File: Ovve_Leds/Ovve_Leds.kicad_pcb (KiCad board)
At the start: 2 copper layers, 100 x 150 mm, 57 parts, among them J1 Conn_01x04, J2 Conn_01x04, J3 Conn_01x04, J4 Conn_01x04, J8 Conn_01x02, U1 74LS174

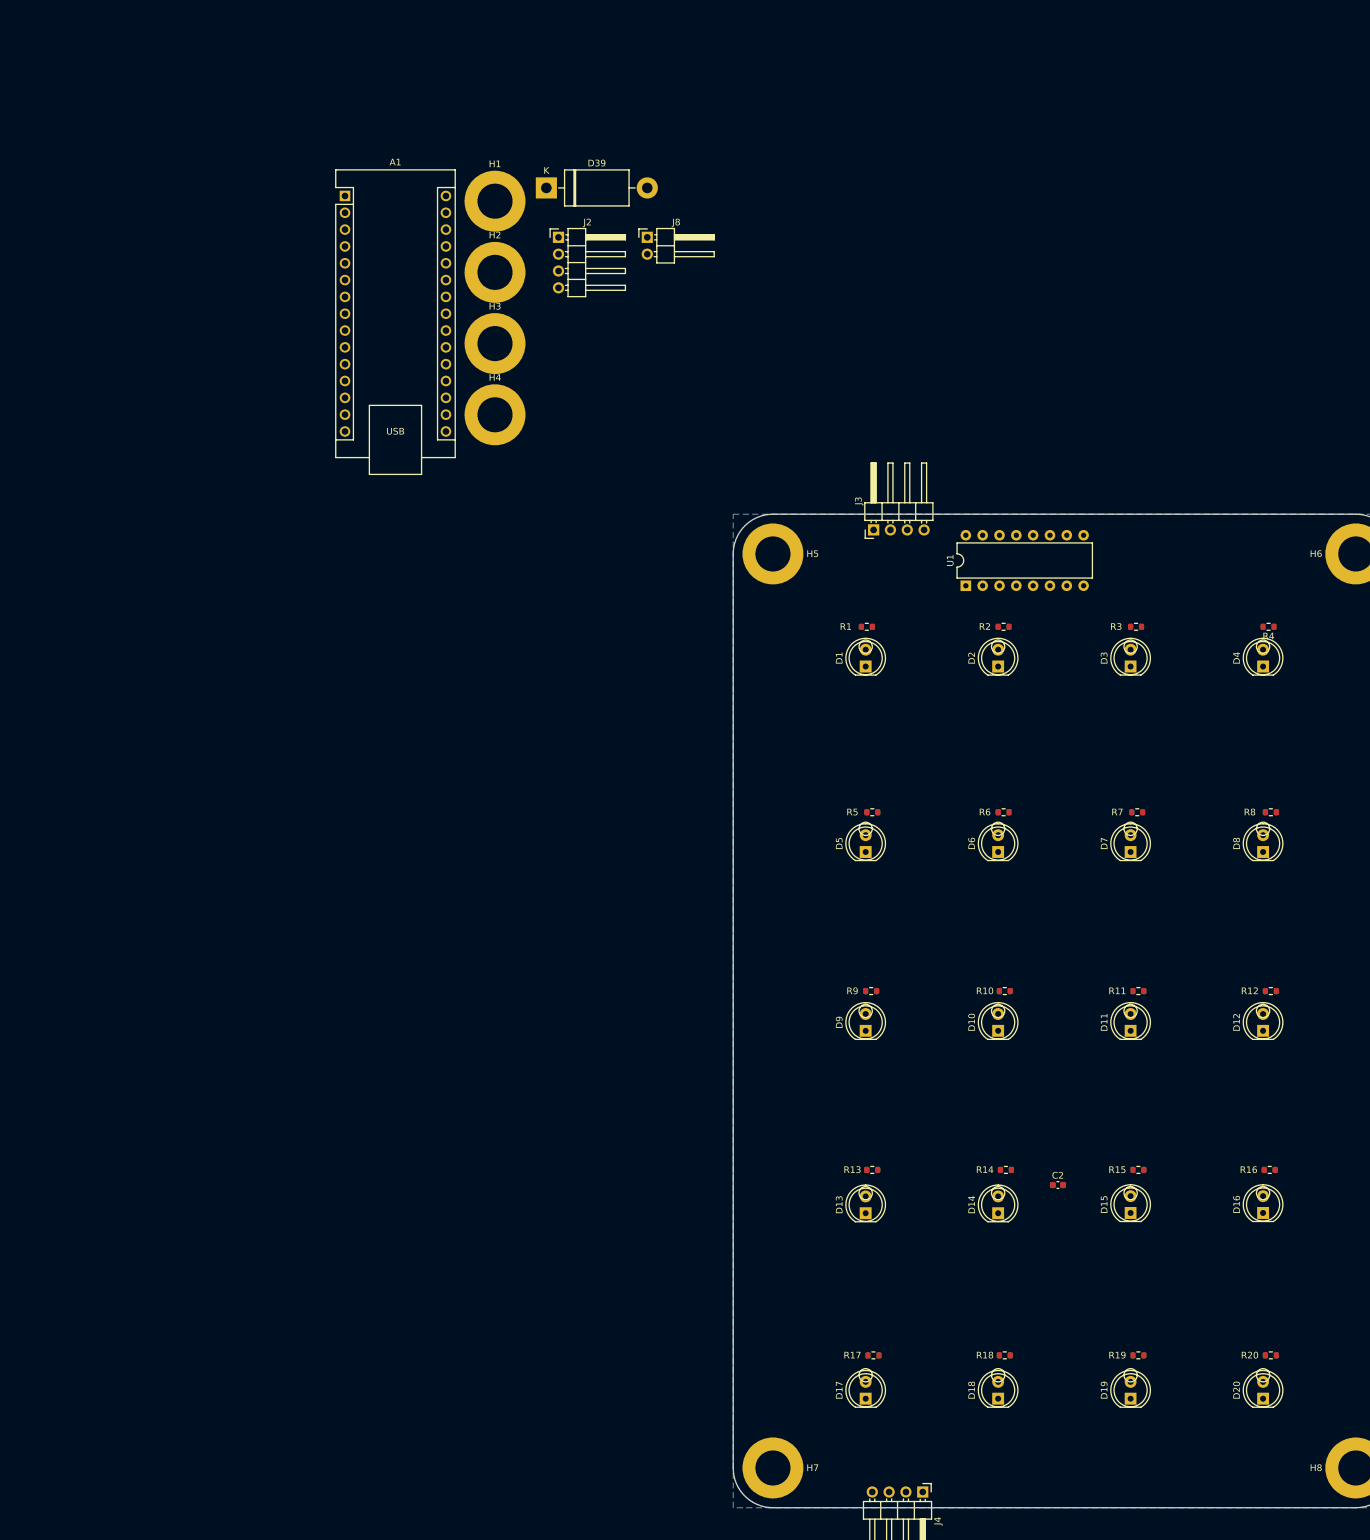
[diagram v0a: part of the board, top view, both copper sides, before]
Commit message: Preliminarily finished with routing letter
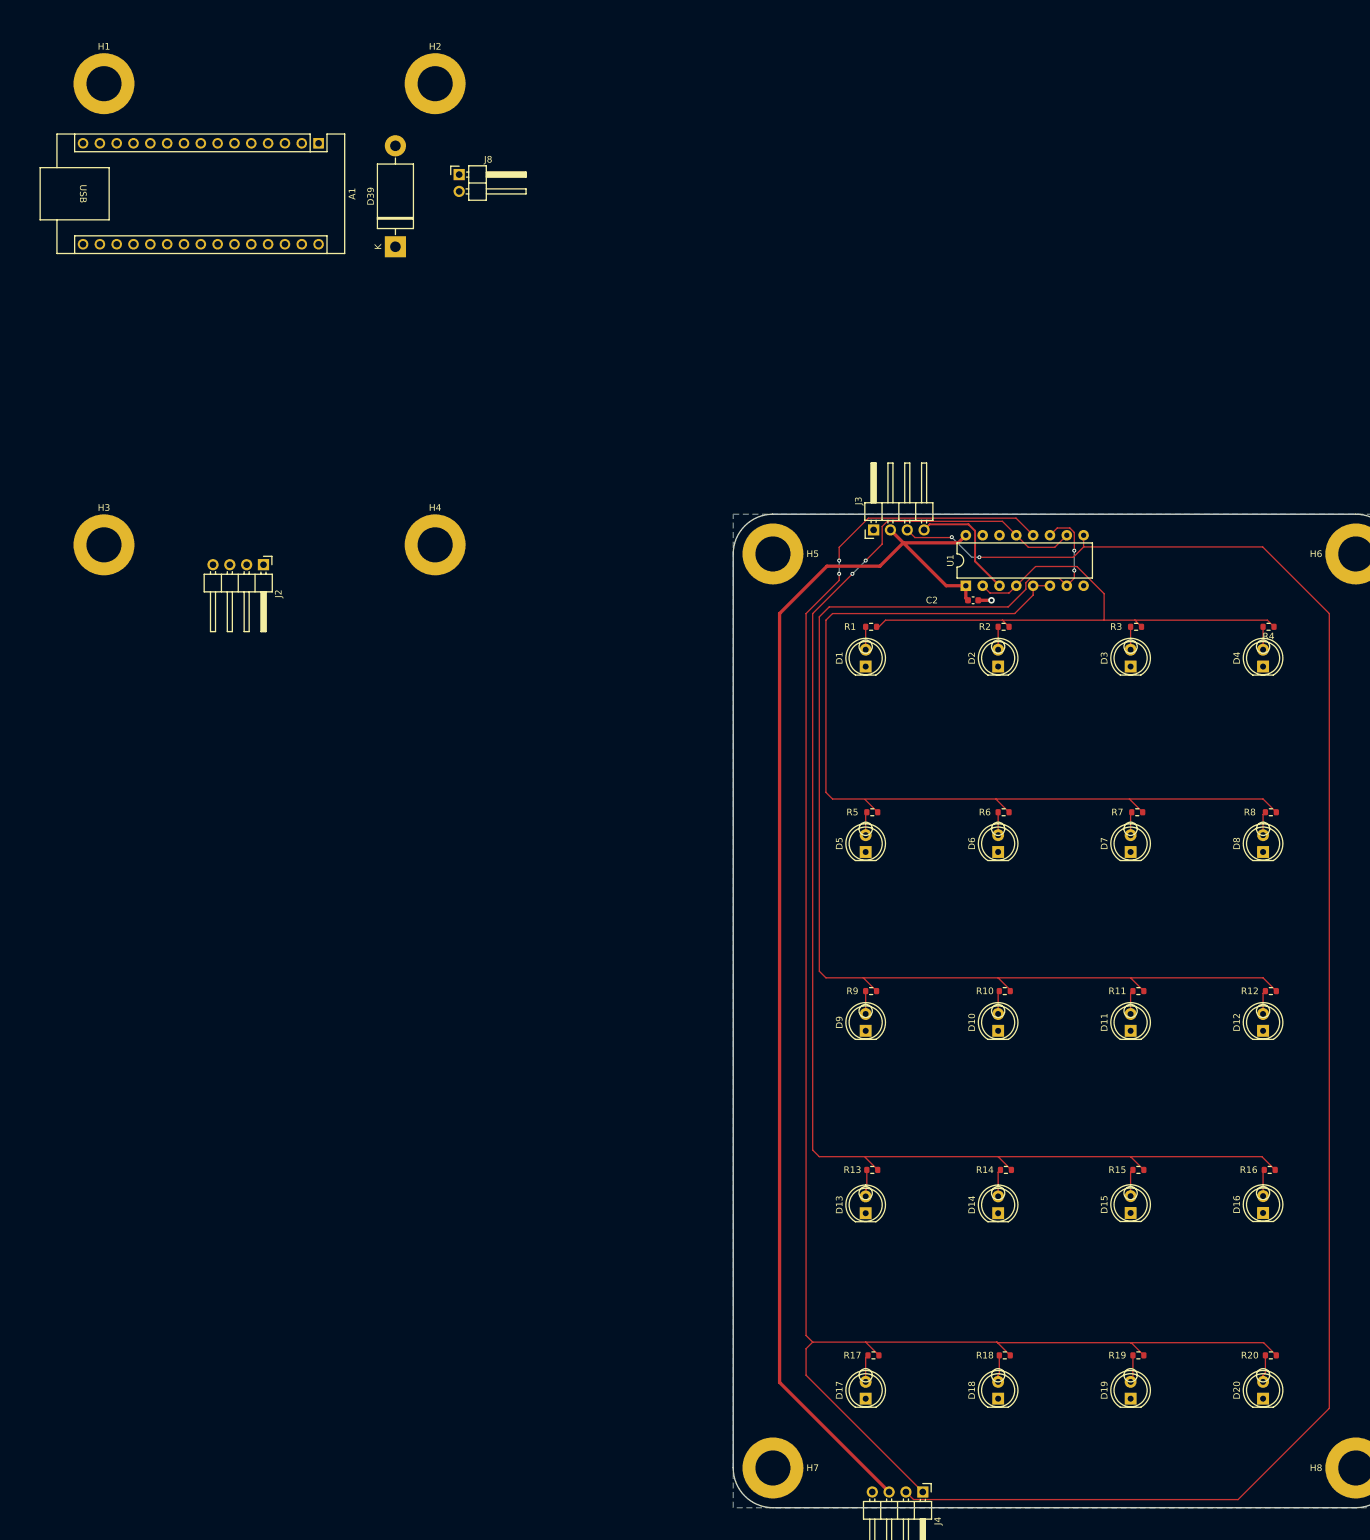
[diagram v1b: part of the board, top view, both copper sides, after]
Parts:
- moved C2 89.2 mm to (241.2, 168.0)
- moved J2 66.5 mm to (134.1, 162.6), turned to -90 degrees
- moved H3 66.4 mm to (110.0, 159.6)
- moved H1 61.6 mm to (110.0, 90.0)
- moved J8 29.9 mm to (163.6, 103.7)
- moved H2 29.9 mm to (160.0, 90.0)
- moved D39 24.5 mm to (154.0, 114.6), turned to 90 degrees
- moved H4 21.6 mm to (160.0, 159.6)
- moved A1 8.90 mm to (142.4, 99.0), turned to -90 degrees
- moved R1 0.65 mm to (225.8, 172.0)
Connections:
- J3 pad 1: /GND_in_A -> GND
- J3 pad 2: /Vcc_in_A -> +5V
- J3 pad 3: /CLK_in_A -> /A_letter/CLK
- J3 pad 4: /DATA_in_A -> /A_letter/DATA
- J4 pad 1: /DATA_out_A -> /A_letter/LED5
- J4 pad 2: /CLK_out_A -> /A_letter/CLK
- J4 pad 3: /Vcc_out_A -> +5V
- J4 pad 4: /GND_out_A -> GND
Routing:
- net /A_letter/LED5: track 0.00 -> 264.3 mm, vias 0 -> 2
- net /A_letter/CLK: track 0.00 -> 262.2 mm, vias 0 -> 2
- net /A_letter/LED4: track 0.00 -> 208.5 mm, vias 0 -> 2
- net +5V: track 0.00 -> 190.8 mm
- net /A_letter/LED3: track 0.00 -> 185.9 mm, vias 0 -> 2
- net /A_letter/LED2: track 0.00 -> 140.4 mm
- net /A_letter/LED1: track 0.00 -> 89.8 mm
- net /A_letter/DATA: track 0.00 -> 18.3 mm
- net Net-(D20-A): track 0.00 -> 4.14 mm
- net Net-(D19-A): track 0.00 -> 4.14 mm
- net Net-(D14-A): track 0.00 -> 4.14 mm
- net Net-(D17-A): track 0.00 -> 4.14 mm
- net Net-(D15-A): track 0.00 -> 4.10 mm
- net Net-(D18-A): track 0.00 -> 4.07 mm
- net Net-(D13-A): track 0.00 -> 4.07 mm
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
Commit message: Finished routing
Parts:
- removed J1: Conn_01x04, Connector_PinHeader_2.54mm:PinHeader_1x04_P2.54mm_Horizontal
- added G***: LOGO, Custom Footprints:pig_10x10, F.Cu at (117.0, 161.3)
- moved J2 91.3 mm to (128.6, 253.8)
- moved H3 90.2 mm to (105.5, 249.8)
- moved H4 90.1 mm to (161.5, 249.8)
- moved H1 71.9 mm to (105.5, 161.8)
- moved H2 71.8 mm to (161.5, 161.8)
- moved J8 70.8 mm to (166.2, 174.5)
- moved A1 70.0 mm to (136.9, 168.8)
- moved D39 68.9 mm to (149.5, 183.4)
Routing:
- net /Arduino_Power_K_letter/DATA: track 0.00 -> 114.3 mm
- net /Arduino_Power_K_letter/CLK: track 0.00 -> 94.1 mm
- net +5V: track 190.8 -> 282.9 mm
- net /Arduino_Power_K_letter/6V_in: track 0.00 -> 20.3 mm
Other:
- board size 100 x 150 mm -> 205.5 x 150 mm
- board text added: "100x150mm"
- board text added: "63x58mm"
- board text added: "68x100mm"
- board text added: "Battery holder 4 x 1.5V"
- board text added: "Karl Ståhlgren"
- board text added: "Ovve LEDs v1 Oktober 2024"
